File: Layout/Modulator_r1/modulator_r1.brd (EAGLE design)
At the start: 75.2 x 49.5 mm, 76 parts, among them Q1 FA-20H, U1 ATMEGA328P-AU, U2 TPS79933QDDCRQ1, U3 CC1125RHBT, U4 MCP1700T-3302E/TT, U5 FT232RL, U6 SIP32509DT-T1-GE3

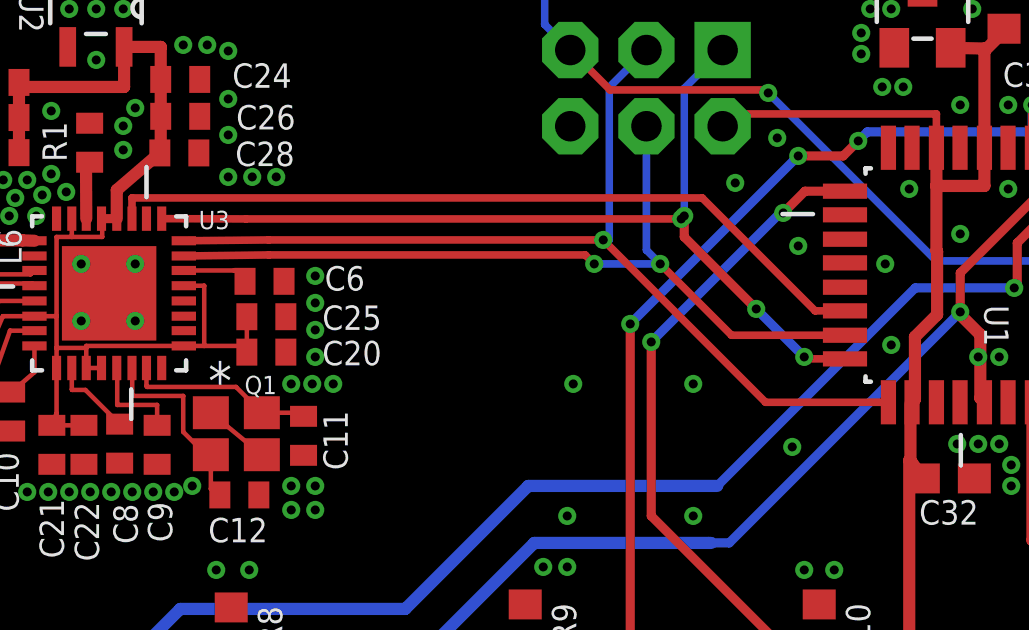
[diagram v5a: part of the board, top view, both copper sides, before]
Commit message: Connected CC_Reset and GPIO0.
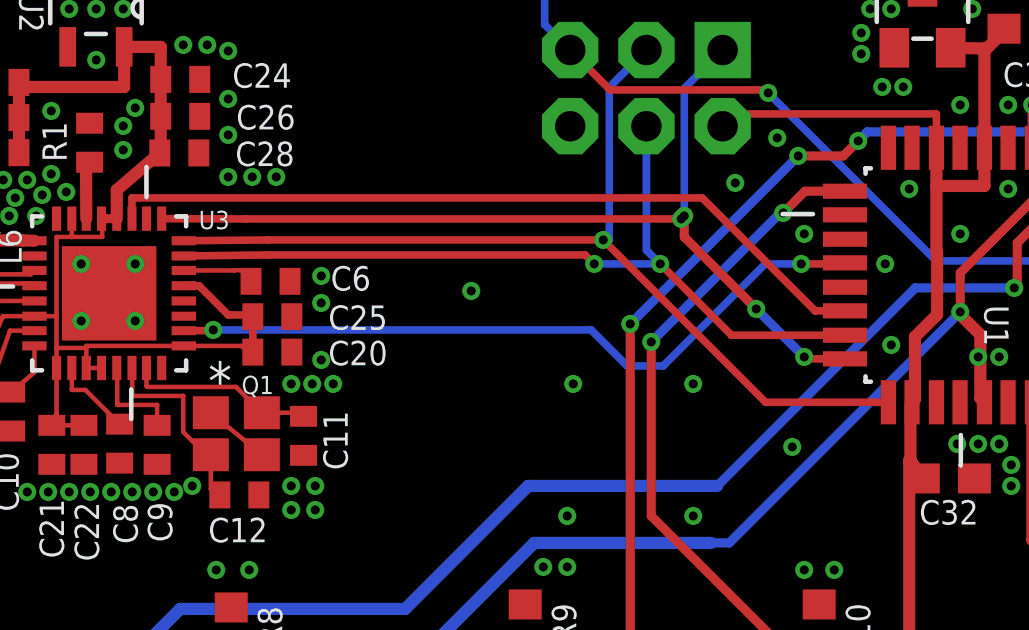
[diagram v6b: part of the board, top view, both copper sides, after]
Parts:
- moved C20 0.20 mm to (25.2, 21.9)
- moved C25 0.20 mm to (25.2, 23.0)
- moved C6 0.20 mm to (25.1, 24.2)
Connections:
- net CC_IO0: now also U1.13
- net CC_NRESET: now also U1.12
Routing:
- net CC_NRESET: track 0.00 -> 24.0 mm, vias 0 -> 2
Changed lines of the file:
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@@
 <attribute name="NAME" x="68.899" y="35.633" size="0.8128" layer="25" rot="R180"/>
 </element>
-<element name="C6" library="resistor" package="C0402" value="220n" x="24.91" y="24.22" smashed="yes">
-<attribute name="NAME" x="26.915" y="23.912" size="0.8128" layer="25"/>
+<element name="C6" library="resistor" package="C0402" value="220n" x="25.11" y="24.22" smashed="yes">
+<attribute name="NAME" x="27.115" y="23.912" size="0.8128" layer="25"/>
 </element>
 <element name="C7" library="resistor" package="C0402" value="10n" x="14.11" y="22.06" smashed="yes" rot="R180">
@@
 </element>
 <element name="Q1" library="crystal" package="FA-20H" value="FA-20H" x="23.97" y="19.14" smashed="yes" rot="R180">
-<attribute name="NAME" x="25.315" y="21.07" size="0.6096" layer="25" rot="R180"/>
+<attribute name="NAME" x="25.215" y="21.07" size="0.6096" layer="25" rot="R180"/>
 </element>
 <element name="C11" library="resistor" package="C0402" value="12p" x="26.21" y="19.07" smashed="yes" rot="R270">
@@
 <attribute name="NAME" x="5.815" y="31.742" size="0.8128" layer="25"/>
 </element>
-<element name="C20" library="resistor" package="C0402" value="47n" x="24.97" y="21.86" smashed="yes">
-<attribute name="NAME" x="26.835" y="21.422" size="0.8128" layer="25"/>
+<element name="C20" library="resistor" package="C0402" value="47n" x="25.17" y="21.86" smashed="yes">
+<attribute name="NAME" x="27.035" y="21.422" size="0.8128" layer="25"/>
 </element>
 <element name="C21" library="resistor" package="C0402" value="47n" x="17.82" y="18.77" smashed="yes" rot="R270">
@@
 <attribute name="NAME" x="23.835" y="30.672" size="0.8128" layer="25"/>
 </element>
-<element name="C25" library="resistor" package="C0402" value="47n" x="24.97" y="23.04" smashed="yes">
-<attribute name="NAME" x="26.835" y="22.602" size="0.8128" layer="25"/>
+<element name="C25" library="resistor" package="C0402" value="47n" x="25.17" y="23.04" smashed="yes">
+<attribute name="NAME" x="27.035" y="22.602" size="0.8128" layer="25"/>
 </element>
 <element name="C26" library="resistor" package="C0402" value="47n" x="22.1" y="29.72" smashed="yes">
@@
 <via x="26.5" y="20.8" extent="1-16" drill="0.3"/>
 <via x="27.2" y="20.8" extent="1-16" drill="0.3"/>
-<via x="26.6" y="22.6" extent="1-16" drill="0.3"/>
-<via x="26.6" y="21.7" extent="1-16" drill="0.3"/>
-<via x="26.6" y="23.5" extent="1-16" drill="0.3"/>
-<via x="26.6" y="24.4" extent="1-16" drill="0.3"/>
+<via x="31.8" y="23.9" extent="1-16" drill="0.3"/>
+<via x="26.8" y="21.6" extent="1-16" drill="0.3"/>
+<via x="26.8" y="23.5" extent="1-16" drill="0.3"/>
+<via x="26.8" y="24.4" extent="1-16" drill="0.3"/>
 <via x="0.6" y="10" extent="1-16" drill="0.3"/>
 <via x="0.5" y="17.9" extent="1-16" drill="0.3"/>
@@
 <via x="45.6" y="24.8" extent="1-16" drill="0.3"/>
 <via x="45.8" y="22.1" extent="1-16" drill="0.3"/>
-<via x="42.7" y="25.4" extent="1-16" drill="0.3"/>
+<via x="42.9" y="25.8" extent="1-16" drill="0.3"/>
 <via x="40.6" y="27.5" extent="1-16" drill="0.3"/>
 <via x="42" y="29" extent="1-16" drill="0.3"/>
@@
 <via x="74.2" y="41.2" extent="1-16" drill="0.3"/>
 <via x="66.5" y="48.3" extent="1-16" drill="0.3"/>
-<wire x1="20.6" y1="22.9" x2="19.73" y2="23.82" width="0" layer="19" extent="1-1"/>
-<wire x1="64.085" y1="27.055" x2="65.5" y2="26.9" width="0" layer="19" extent="1-1"/>
 <via x="2.5" y="34.5" extent="1-16" drill="0.3"/>
 <via x="2.5" y="26.6" extent="1-16" drill="0.3"/>
@@
 <via x="0.6" y="20" extent="1-16" drill="0.3"/>
 <via x="0.6" y="7" extent="1-16" drill="0.3"/>
+<wire x1="20.6" y1="22.9" x2="19.73" y2="23.82" width="0" layer="19" extent="1-1"/>
+<wire x1="64.085" y1="27.055" x2="65.5" y2="26.9" width="0" layer="19" extent="1-1"/>
 </signal>
 <signal name="VCCIO">
@@
 <wire x1="18.4854" y1="25.7" x2="17.9774" y2="25.7" width="0.1524" layer="1"/>
 <wire x1="17.9774" y1="25.7" x2="17.9774" y2="23.058" width="0.1524" layer="1"/>
-<wire x1="24.32" y1="21.86" x2="24.32" y2="23.04" width="0.1524" layer="1"/>
-<wire x1="24.32" y1="21.86" x2="24.1126" y2="22.0674" width="0.1524" layer="1"/>
-<wire x1="24.1126" y1="22.0674" x2="22.9" y2="22.0674" width="0.1524" layer="1"/>
-<wire x1="22.9" y1="22.0674" x2="22.2192" y2="22.0674" width="0.1524" layer="1"/>
-<wire x1="22.2192" y1="24.074" x2="22.9" y2="24.074" width="0.1524" layer="1"/>
-<wire x1="22.9" y1="24.074" x2="22.9" y2="22.0674" width="0.1524" layer="1"/>
+<wire x1="24.52" y1="21.86" x2="24.1126" y2="22.0674" width="0.1524" layer="1"/>
+<wire x1="24.1126" y1="22.0674" x2="22.2192" y2="22.0674" width="0.1524" layer="1"/>
 <wire x1="22.2192" y1="22.0674" x2="18.968" y2="22.0674" width="0.1524" layer="1"/>
 <wire x1="18.968" y1="22.0674" x2="18.968" y2="22" width="0.1524" layer="1"/>
@@
 <wire x1="14.75" y1="20.98" x2="14.75" y2="19.96" width="0.1524" layer="1"/>
 <wire x1="14.75" y1="19.96" x2="14.74" y2="19.95" width="0.1524" layer="1"/>
+<wire x1="22.2192" y1="24.074" x2="22.726" y2="24.074" width="0.254" layer="1"/>
+<wire x1="22.726" y1="24.074" x2="23.7" y2="23.1" width="0.254" layer="1"/>
+<wire x1="23.7" y1="23.1" x2="24.46" y2="23.1" width="0.254" layer="1"/>
+<wire x1="24.46" y1="23.1" x2="24.52" y2="23.04" width="0.254" layer="1"/>
+<wire x1="24.52" y1="23.04" x2="24.52" y2="21.86" width="0.254" layer="1"/>
 </signal>
 <signal name="N$8">
@@
 <contactref element="C6" pad="1"/>
 <wire x1="22.2192" y1="24.582" x2="23.898" y2="24.582" width="0.1524" layer="1"/>
-<wire x1="23.898" y1="24.582" x2="24.26" y2="24.22" width="0.1524" layer="1" curve="-90"/>
+<wire x1="23.898" y1="24.582" x2="24.46" y2="24.22" width="0.1524" layer="1" curve="-90"/>
 </signal>
 <signal name="CC_IO3">
@@
 <signal name="CC_IO0">
 <contactref element="U3" pad="10"/>
+<contactref element="U1" pad="13"/>
+<wire x1="20.9746" y1="26.3092" x2="44.2582" y2="24.0236" width="0" layer="19" extent="1-1"/>
 </signal>
 <signal name="CC_NRESET">
 <contactref element="U3" pad="2"/>
+<contactref element="U1" pad="12"/>
+<wire x1="22.2192" y1="22.5754" x2="23" y2="22.5754" width="0.254" layer="1"/>
+<wire x1="23" y1="22.5754" x2="23.2" y2="22.6" width="0.254" layer="1"/>
+<via x="23.2" y="22.6" extent="1-16" drill="0.3"/>
+<wire x1="23.2" y1="22.6" x2="35.8" y2="22.6" width="0.254" layer="16"/>
+<wire x1="35.8" y1="22.6" x2="37" y2="21.4" width="0.254" layer="16"/>
+<wire x1="37" y1="21.4" x2="38.2" y2="21.4" width="0.254" layer="16"/>
+<wire x1="38.2" y1="21.4" x2="41.6" y2="24.8" width="0.254" layer="16"/>
+<wire x1="41.6" y1="24.8" x2="42.8" y2="24.8" width="0.254" layer="16"/>
+<via x="42.8" y="24.8" extent="1-16" drill="0.3"/>
+<wire x1="42.8" y1="24.8" x2="44.2218" y2="24.8" width="0.254" layer="1"/>
+<wire x1="44.2218" y1="24.8" x2="44.2582" y2="24.8364" width="0.254" layer="1"/>
 </signal>
 <signal name="N$7">

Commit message: Clear up DRC errors.
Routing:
- net CC_IO0: track 0.00 -> 26.1 mm, vias 0 -> 2
- net GND: track 5.47 -> 2.20 mm
- net CC_VDD: track 45.0 -> 45.9 mm
- net NSS: track 26.0 -> 26.9 mm
- net MISO: track 31.3 -> 32.0 mm, vias 4 -> 3

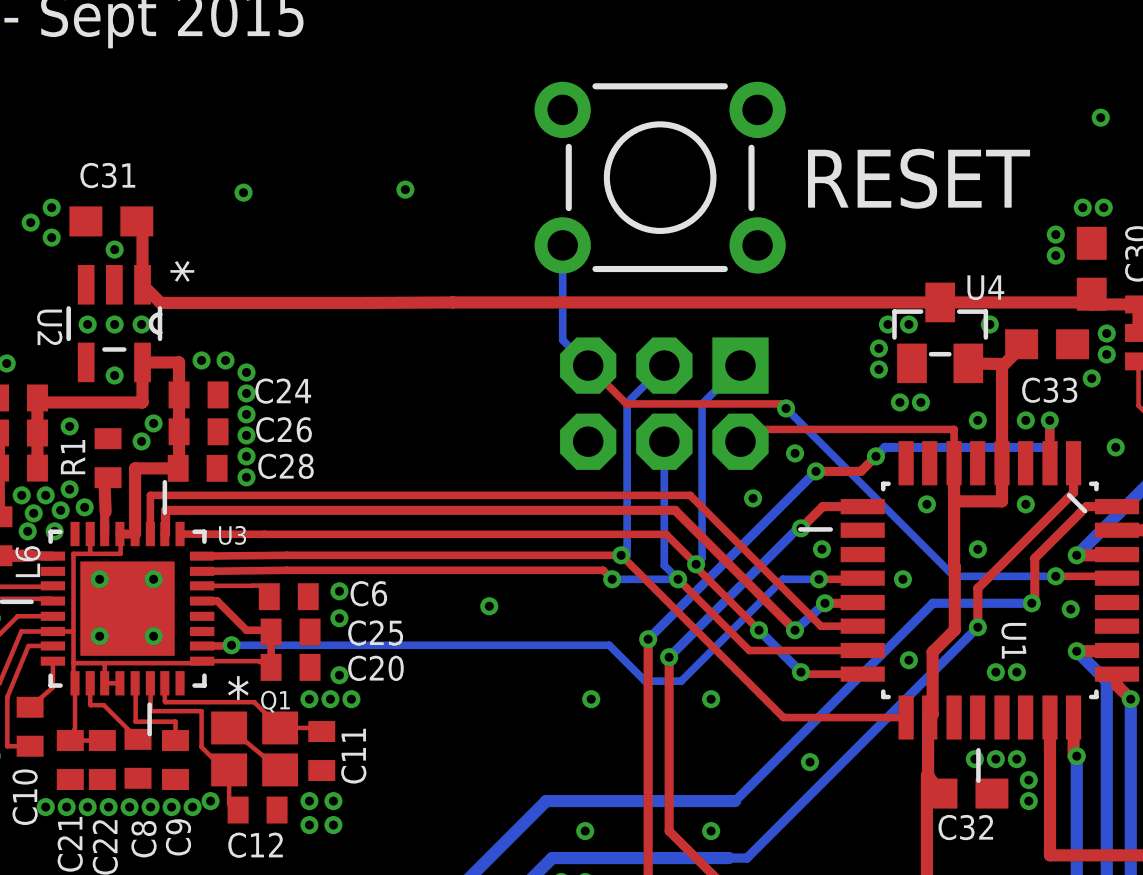
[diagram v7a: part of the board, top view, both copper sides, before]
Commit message: Connect GPIO2/3.
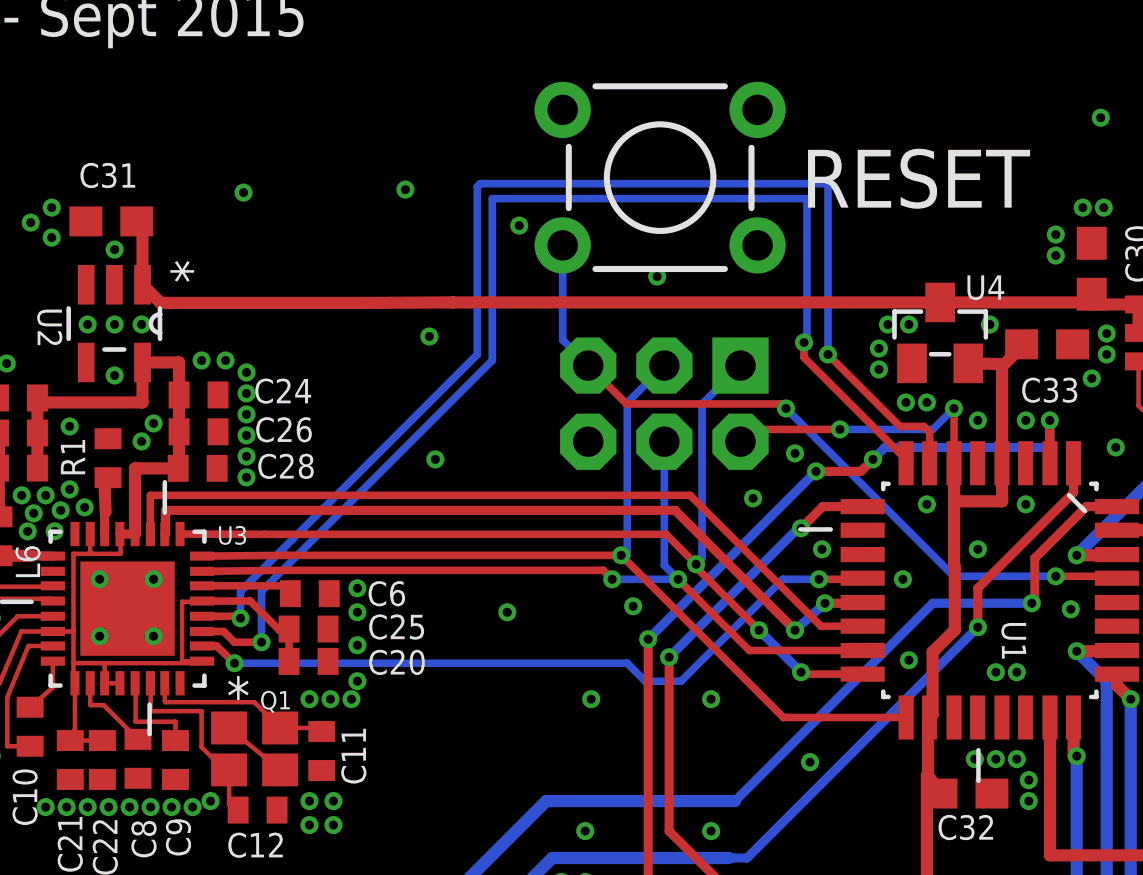
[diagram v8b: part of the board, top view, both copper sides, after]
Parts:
- moved C6 0.71 mm to (25.8, 24.3)
- moved C20 0.63 mm to (25.8, 22.1)
- moved C25 0.61 mm to (25.8, 23.1)
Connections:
- net CC_IO2: now also U1.7
- net CC_IO3: now also U1.8
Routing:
- net CC_IO2: track 0.00 -> 41.9 mm, vias 0 -> 2
- net CC_IO3: track 0.00 -> 40.9 mm, vias 0 -> 2
- net CC_VDD: track 45.9 -> 47.4 mm
- net +3V3: track 76.6 -> 77.6 mm, vias 0 -> 2
- net N$11: track 2.35 -> 3.32 mm
- net GND: vias 320 -> 326
